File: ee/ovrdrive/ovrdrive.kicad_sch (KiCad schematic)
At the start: 53 parts, among them J2 USB3_A, J4 Micro_SD_Card_Det_Hirose_DM3AT, SW1 SW_Push, U1 CH569W, U2 TLV62569DBV, U3 TLV62569DBV, Y2 30Mhz

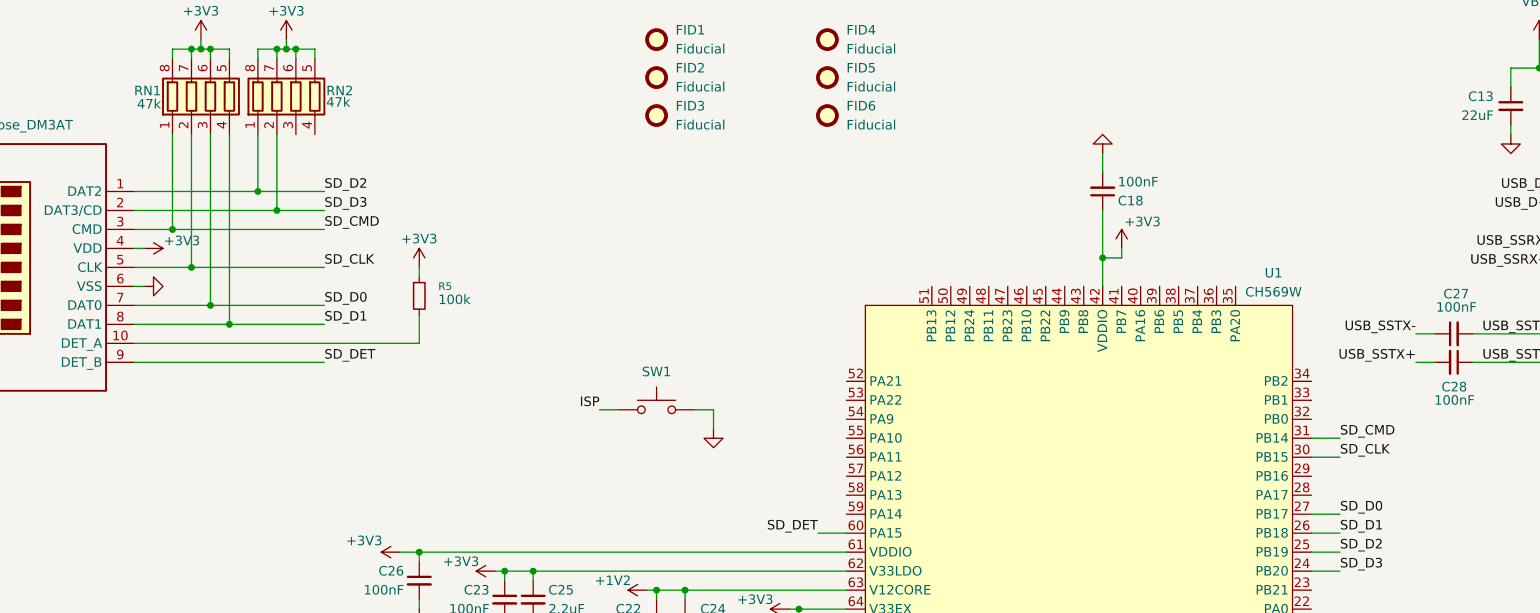
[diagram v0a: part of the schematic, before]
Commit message: Fixed SDIO pinout, length matched SDIO traces.
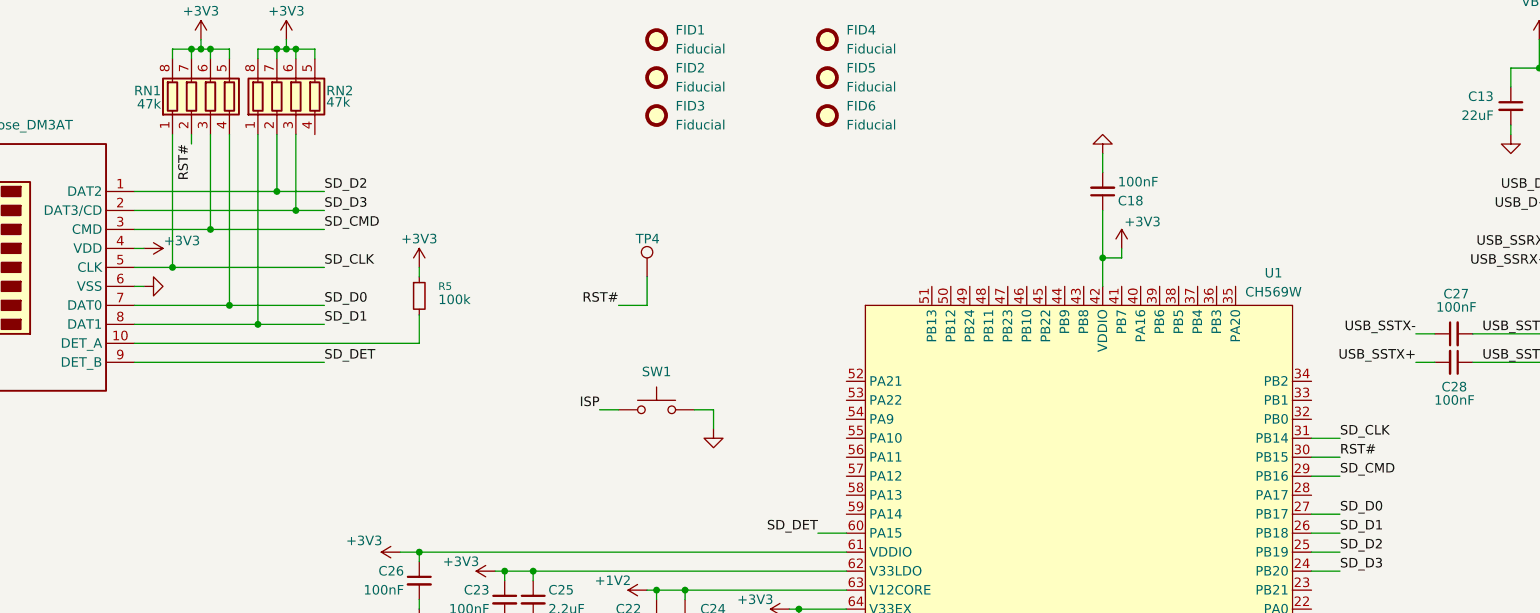
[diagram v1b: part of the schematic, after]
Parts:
- added TP4: TestPoint, TestPoint:TestPoint_Pad_1.0x1.0mm, symbol Connector:TestPoint
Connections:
- net SD_CLK: now also RN1.1 (R1.1), U1.31 (PB14); no longer RN1.2 (R2.1), U1.30 (PB15)
- net SD_CMD: now also RN1.3 (R3.1), U1.29 (PB16); no longer RN1.1 (R1.1), U1.31 (PB14)
- net SD_D0: now also RN1.4 (R4.1); no longer RN1.3 (R3.1)
- net SD_D1: now also RN2.1 (R1.1); no longer RN1.4 (R4.1)
- net SD_D2: now also RN2.2 (R2.1); no longer RN2.1 (R1.1)
- net SD_D3: now also RN2.3 (R3.1); no longer RN2.2 (R2.1)
- new net RST#: RN1.2 (R2.1), TP4.1, U1.30 (PB15)
